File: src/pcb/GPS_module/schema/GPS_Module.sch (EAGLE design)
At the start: 8 parts, among them J1 U.FL-R-SMT-1(10), U1 SL876Q5A001T001000

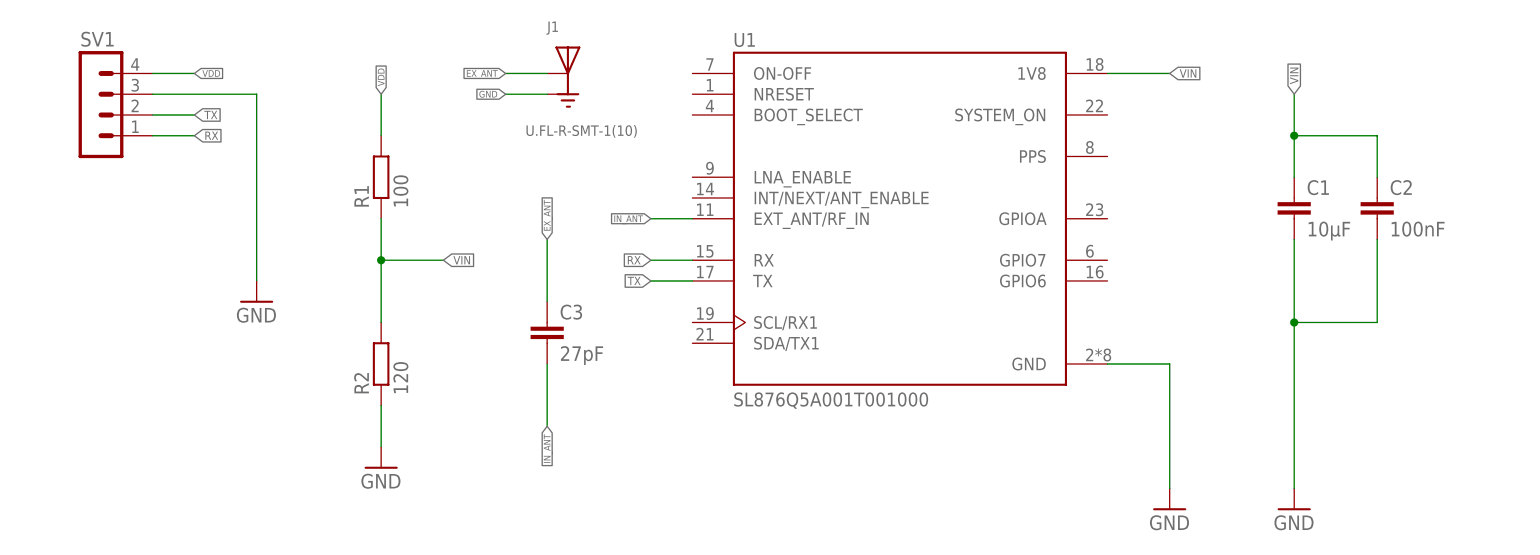
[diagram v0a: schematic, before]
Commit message: Updated GPS Module, Footprints, Automatic backups
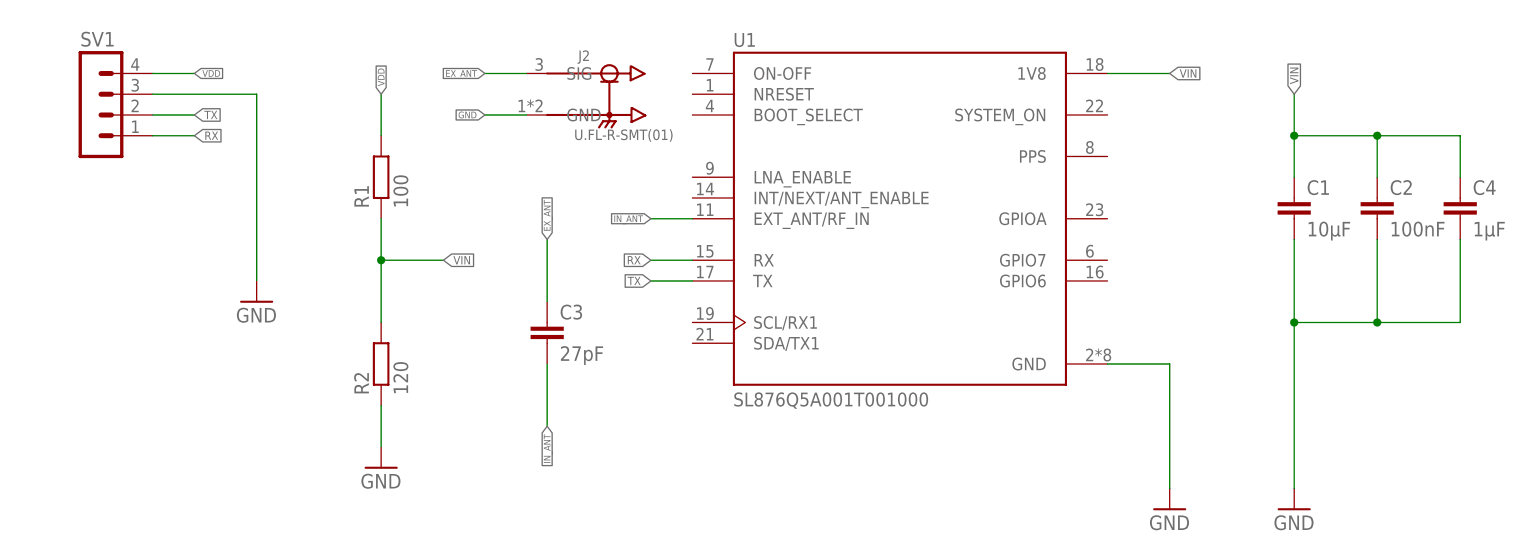
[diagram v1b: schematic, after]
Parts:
- removed J1: U.FL-R-SMT-1(10), U.FL-R-SMT-1_10_:U.FL-R-SMT-1(10)
- added C4: 1µF, rcl:C-EUC0805
- added J2: U.FL-R-SMT(01), U.FL-R-SMT_01_:U.FL-R-SMT(01)
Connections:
- net EX_ANT: now also J2.SIG; no longer J1.SIG
- net GND: now also C4.2, J2.GND; no longer J1.GND
- net VIN: now also C4.1
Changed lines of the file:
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@@
 <part name="GND4" library="supply1" library_urn="urn:adsk.eagle:library:371" deviceset="GND" device=""/>
 <part name="GND2" library="supply1" library_urn="urn:adsk.eagle:library:371" deviceset="GND" device=""/>
-<part name="J1" library="U.FL-R-SMT-1_10_" deviceset="U.FL-R-SMT-1(10)" device=""/>
 <part name="C3" library="rcl" library_urn="urn:adsk.eagle:library:334" deviceset="C-EU" device="C0805" package3d_urn="urn:adsk.eagle:package:23617/2" value="27pF"/>
+<part name="J2" library="U.FL-R-SMT_01_" deviceset="U.FL-R-SMT(01)" device=""/>
+<part name="C4" library="rcl" library_urn="urn:adsk.eagle:library:334" deviceset="C-EU" device="C0805" package3d_urn="urn:adsk.eagle:package:23617/2" value="1µF"/>
 </parts>
 <sheets>
@@
 <attribute name="VALUE" x="-119.38" y="-66.04" size="1.778" layer="96"/>
 </instance>
-<instance part="J1" gate="G$1" x="-93.98" y="-15.24" smashed="yes">
-<attribute name="NAME" x="-96.52058125" y="-10.153059375" size="1.27303125" layer="95"/>
-<attribute name="VALUE" x="-99.18773125" y="-22.87458125" size="1.27435" layer="96"/>
-</instance>
 <instance part="C3" gate="G$1" x="-96.52" y="-45.72" smashed="yes">
 <attribute name="NAME" x="-94.996" y="-45.339" size="1.778" layer="95"/>
 <attribute name="VALUE" x="-94.996" y="-50.419" size="1.778" layer="96"/>
+</instance>
+<instance part="J2" gate="G$1" x="-88.9" y="-17.78" smashed="yes">
+<attribute name="NAME" x="-92.71856875" y="-13.70686875" size="1.27285" layer="95"/>
+<attribute name="VALUE" x="-93.22781875" y="-23.3807" size="1.27288125" layer="96"/>
+</instance>
+<instance part="C4" gate="G$1" x="15.24" y="-30.48" smashed="yes">
+<attribute name="NAME" x="16.764" y="-30.099" size="1.778" layer="95"/>
+<attribute name="VALUE" x="16.764" y="-35.179" size="1.778" layer="96"/>
 </instance>
 </instances>
@@
 <pinref part="C1" gate="G$1" pin="1"/>
 <pinref part="C2" gate="G$1" pin="1"/>
+<pinref part="C4" gate="G$1" pin="1"/>
+<wire x1="15.24" y1="-27.94" x2="15.24" y2="-22.86" width="0.1524" layer="91"/>
+<wire x1="15.24" y1="-22.86" x2="5.08" y2="-22.86" width="0.1524" layer="91"/>
+<junction x="5.08" y="-22.86"/>
 </segment>
 </net>
@@
 <pinref part="C2" gate="G$1" pin="2"/>
 <pinref part="GND4" gate="1" pin="GND"/>
+<pinref part="C4" gate="G$1" pin="2"/>
+<wire x1="15.24" y1="-35.56" x2="15.24" y2="-45.72" width="0.1524" layer="91"/>
+<wire x1="15.24" y1="-45.72" x2="5.08" y2="-45.72" width="0.1524" layer="91"/>
+<junction x="5.08" y="-45.72"/>
 </segment>
 <segment>
-<pinref part="J1" gate="G$1" pin="GND"/>
-<wire x1="-96.52" y1="-17.78" x2="-101.6" y2="-17.78" width="0.1524" layer="91"/>
-<label x="-101.6" y="-17.78" size="0.8128" layer="95" rot="R180" xref="yes"/>
+<wire x1="-99.06" y1="-20.32" x2="-104.14" y2="-20.32" width="0.1524" layer="91"/>
+<label x="-104.14" y="-20.32" size="0.8128" layer="95" rot="R180" xref="yes"/>
+<pinref part="J2" gate="G$1" pin="GND"/>
 </segment>
 </net>
@@
 </segment>
 <segment>
-<pinref part="J1" gate="G$1" pin="SIG"/>
-<wire x1="-96.52" y1="-15.24" x2="-101.6" y2="-15.24" width="0.1524" layer="91"/>
-<label x="-101.6" y="-15.24" size="0.8128" layer="95" rot="R180" xref="yes"/>
+<wire x1="-99.06" y1="-15.24" x2="-104.14" y2="-15.24" width="0.1524" layer="91"/>
+<label x="-104.14" y="-15.24" size="0.8128" layer="95" rot="R180" xref="yes"/>
+<pinref part="J2" gate="G$1" pin="SIG"/>
 </segment>
 </net>

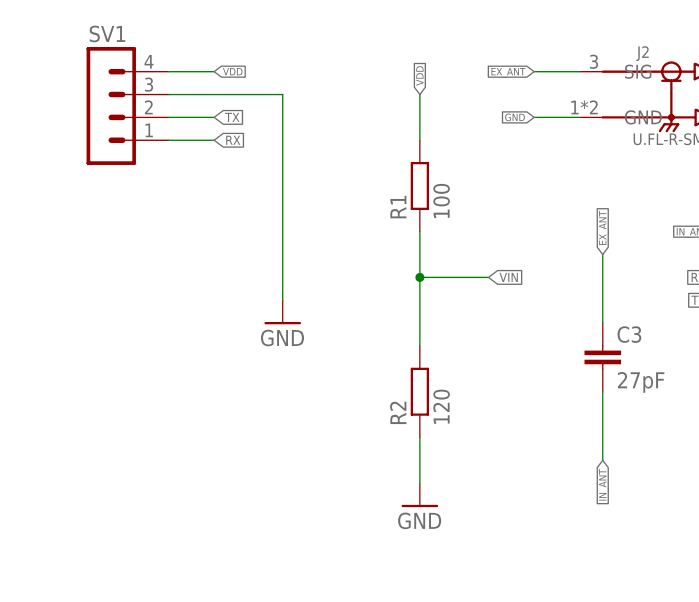
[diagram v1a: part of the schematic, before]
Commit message: updated shematic of GPS and Humidity
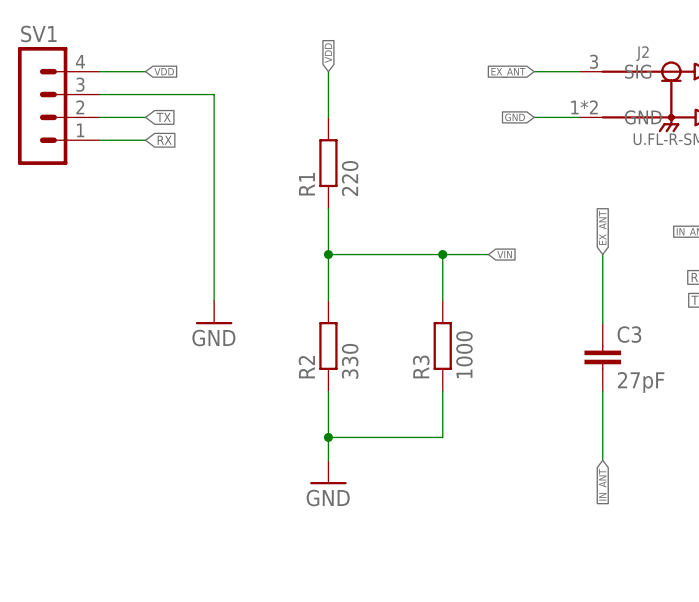
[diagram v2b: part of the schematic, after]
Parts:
- added R3: 1000, rcl:R-EU_R0402
- R1: value 100 -> 220; device rcl:R-EU_R0805 -> rcl:R-EU_R0402
- R2: value 120 -> 330; device rcl:R-EU_R0805 -> rcl:R-EU_R0402
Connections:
- net GND: now also R3.1
- net VIN: now also R3.2
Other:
- moved on the sheet: R1, R2, SV1
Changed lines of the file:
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@@
 <part name="U1" library="SL876Q5A001T001000" deviceset="SL876Q5A001T001000" device=""/>
 <part name="SV1" library="con-lstb" library_urn="urn:adsk.eagle:library:162" deviceset="MA04-1" device="" package3d_urn="urn:adsk.eagle:package:8337/1"/>
-<part name="R1" library="rcl" library_urn="urn:adsk.eagle:library:334" deviceset="R-EU_" device="R0805" package3d_urn="urn:adsk.eagle:package:23553/2" value="100"/>
-<part name="R2" library="rcl" library_urn="urn:adsk.eagle:library:334" deviceset="R-EU_" device="R0805" package3d_urn="urn:adsk.eagle:package:23553/2" value="120"/>
+<part name="R1" library="rcl" library_urn="urn:adsk.eagle:library:334" deviceset="R-EU_" device="R0402" package3d_urn="urn:adsk.eagle:package:23547/3" value="220"/>
+<part name="R2" library="rcl" library_urn="urn:adsk.eagle:library:334" deviceset="R-EU_" device="R0402" package3d_urn="urn:adsk.eagle:package:23547/3" value="330"/>
 <part name="C1" library="rcl" library_urn="urn:adsk.eagle:library:334" deviceset="C-EU" device="C0805" package3d_urn="urn:adsk.eagle:package:23617/2" value="10µF"/>
 <part name="C2" library="rcl" library_urn="urn:adsk.eagle:library:334" deviceset="C-EU" device="C0805" package3d_urn="urn:adsk.eagle:package:23617/2" value="100nF"/>
@@
 <part name="J2" library="U.FL-R-SMT_01_" deviceset="U.FL-R-SMT(01)" device=""/>
 <part name="C4" library="rcl" library_urn="urn:adsk.eagle:library:334" deviceset="C-EU" device="C0805" package3d_urn="urn:adsk.eagle:package:23617/2" value="1µF"/>
+<part name="R3" library="rcl" library_urn="urn:adsk.eagle:library:334" deviceset="R-EU_" device="R0402" package3d_urn="urn:adsk.eagle:package:23547/3" value="1000"/>
 </parts>
 <sheets>
@@
 <attribute name="VALUE" x="-73.7559" y="-55.9878" size="1.684309375" layer="96"/>
 </instance>
-<instance part="SV1" gate="1" x="-152.4" y="-17.78" smashed="yes">
-<attribute name="VALUE" x="-153.67" y="-27.94" size="1.778" layer="96"/>
-<attribute name="NAME" x="-153.67" y="-11.938" size="1.778" layer="95"/>
+<instance part="SV1" gate="1" x="-160.02" y="-17.78" smashed="yes">
+<attribute name="VALUE" x="-161.29" y="-27.94" size="1.778" layer="96"/>
+<attribute name="NAME" x="-161.29" y="-11.938" size="1.778" layer="95"/>
 </instance>
-<instance part="R1" gate="G$1" x="-116.84" y="-27.94" smashed="yes" rot="R90">
-<attribute name="NAME" x="-118.3386" y="-31.75" size="1.778" layer="95" rot="R90"/>
-<attribute name="VALUE" x="-113.538" y="-31.75" size="1.778" layer="96" rot="R90"/>
+<instance part="R1" gate="G$1" x="-127" y="-25.4" smashed="yes" rot="R90">
+<attribute name="NAME" x="-128.4986" y="-29.21" size="1.778" layer="95" rot="R90"/>
+<attribute name="VALUE" x="-123.698" y="-29.21" size="1.778" layer="96" rot="R90"/>
 </instance>
-<instance part="R2" gate="G$1" x="-116.84" y="-50.8" smashed="yes" rot="R90">
-<attribute name="NAME" x="-118.3386" y="-54.61" size="1.778" layer="95" rot="R90"/>
-<attribute name="VALUE" x="-113.538" y="-54.61" size="1.778" layer="96" rot="R90"/>
+<instance part="R2" gate="G$1" x="-127" y="-45.72" smashed="yes" rot="R90">
+<attribute name="NAME" x="-128.4986" y="-49.53" size="1.778" layer="95" rot="R90"/>
+<attribute name="VALUE" x="-123.698" y="-49.53" size="1.778" layer="96" rot="R90"/>
 </instance>
 <instance part="C1" gate="G$1" x="-5.08" y="-30.48" smashed="yes">
@@
 <attribute name="VALUE" x="6.604" y="-35.179" size="1.778" layer="96"/>
 </instance>
-<instance part="GND1" gate="1" x="-132.08" y="-43.18" smashed="yes">
-<attribute name="VALUE" x="-134.62" y="-45.72" size="1.778" layer="96"/>
+<instance part="GND1" gate="1" x="-139.7" y="-43.18" smashed="yes">
+<attribute name="VALUE" x="-142.24" y="-45.72" size="1.778" layer="96"/>
 </instance>
 <instance part="GND3" gate="1" x="-20.32" y="-68.58" smashed="yes">
@@
 <attribute name="VALUE" x="-7.62" y="-71.12" size="1.778" layer="96"/>
 </instance>
-<instance part="GND2" gate="1" x="-116.84" y="-63.5" smashed="yes">
-<attribute name="VALUE" x="-119.38" y="-66.04" size="1.778" layer="96"/>
+<instance part="GND2" gate="1" x="-127" y="-60.96" smashed="yes">
+<attribute name="VALUE" x="-129.54" y="-63.5" size="1.778" layer="96"/>
 </instance>
 <instance part="C3" gate="G$1" x="-96.52" y="-45.72" smashed="yes">
@@
 <attribute name="VALUE" x="16.764" y="-35.179" size="1.778" layer="96"/>
 </instance>
+<instance part="R3" gate="G$1" x="-114.3" y="-45.72" smashed="yes" rot="R90">
+<attribute name="NAME" x="-115.7986" y="-49.53" size="1.778" layer="95" rot="R90"/>
+<attribute name="VALUE" x="-110.998" y="-49.53" size="1.778" layer="96" rot="R90"/>
+</instance>
 </instances>
 <busses>
@@
 </segment>
 <segment>
-<wire x1="-144.78" y1="-20.32" x2="-139.7" y2="-20.32" width="0.1524" layer="91"/>
-<label x="-139.7" y="-20.32" size="1.016" layer="95" xref="yes"/>
+<wire x1="-152.4" y1="-20.32" x2="-147.32" y2="-20.32" width="0.1524" layer="91"/>
+<label x="-147.32" y="-20.32" size="1.016" layer="95" xref="yes"/>
 <pinref part="SV1" gate="1" pin="2"/>
 </segment>
@@
 <net name="VDD" class="0">
 <segment>
-<label x="-116.84" y="-17.78" size="0.8128" layer="95" rot="R90" xref="yes"/>
+<label x="-127" y="-15.24" size="0.8128" layer="95" rot="R90" xref="yes"/>
 <pinref part="R1" gate="G$1" pin="2"/>
-<wire x1="-116.84" y1="-22.86" x2="-116.84" y2="-17.78" width="0.1524" layer="91"/>
+<wire x1="-127" y1="-20.32" x2="-127" y2="-15.24" width="0.1524" layer="91"/>
 </segment>
 <segment>
-<wire x1="-144.78" y1="-15.24" x2="-139.7" y2="-15.24" width="0.1524" layer="91"/>
-<label x="-139.7" y="-15.24" size="0.8128" layer="95" xref="yes"/>
+<wire x1="-152.4" y1="-15.24" x2="-147.32" y2="-15.24" width="0.1524" layer="91"/>
+<label x="-147.32" y="-15.24" size="0.8128" layer="95" xref="yes"/>
 <pinref part="SV1" gate="1" pin="4"/>
 </segment>
@@
 </segment>
 <segment>
-<junction x="-116.84" y="-38.1"/>
-<wire x1="-116.84" y1="-33.02" x2="-116.84" y2="-38.1" width="0.1524" layer="91"/>
-<wire x1="-116.84" y1="-38.1" x2="-116.84" y2="-45.72" width="0.1524" layer="91"/>
-<wire x1="-116.84" y1="-38.1" x2="-109.22" y2="-38.1" width="0.1524" layer="91"/>
-<label x="-109.22" y="-38.1" size="1.016" layer="95" xref="yes"/>
+<wire x1="-127" y1="-30.48" x2="-127" y2="-35.56" width="0.1524" layer="91"/>
 <pinref part="R1" gate="G$1" pin="1"/>
 <pinref part="R2" gate="G$1" pin="2"/>
+<pinref part="R3" gate="G$1" pin="2"/>
+<wire x1="-127" y1="-35.56" x2="-127" y2="-40.64" width="0.1524" layer="91"/>
+<wire x1="-114.3" y1="-40.64" x2="-114.3" y2="-35.56" width="0.1524" layer="91"/>
+<wire x1="-114.3" y1="-35.56" x2="-127" y2="-35.56" width="0.1524" layer="91"/>
+<junction x="-127" y="-35.56"/>
+<junction x="-114.3" y="-35.56"/>
+<wire x1="-114.3" y1="-35.56" x2="-109.22" y2="-35.56" width="0.1524" layer="91"/>
+<label x="-109.22" y="-35.56" size="0.8128" layer="95" xref="yes"/>
 </segment>
 <segment>
@@
 <net name="RX" class="0">
 <segment>
-<wire x1="-144.78" y1="-22.86" x2="-139.7" y2="-22.86" width="0.1524" layer="91"/>
-<label x="-139.7" y="-22.86" size="1.016" layer="95" xref="yes"/>
+<wire x1="-152.4" y1="-22.86" x2="-147.32" y2="-22.86" width="0.1524" layer="91"/>
+<label x="-147.32" y="-22.86" size="1.016" layer="95" xref="yes"/>
 <pinref part="SV1" gate="1" pin="1"/>
 </segment>
@@
 <net name="GND" class="0">
 <segment>
-<wire x1="-144.78" y1="-17.78" x2="-132.08" y2="-17.78" width="0.1524" layer="91"/>
-<wire x1="-132.08" y1="-17.78" x2="-132.08" y2="-40.64" width="0.1524" layer="91"/>
+<wire x1="-152.4" y1="-17.78" x2="-139.7" y2="-17.78" width="0.1524" layer="91"/>
+<wire x1="-139.7" y1="-17.78" x2="-139.7" y2="-40.64" width="0.1524" layer="91"/>
 <pinref part="SV1" gate="1" pin="3"/>
 <pinref part="GND1" gate="1" pin="GND"/>
@@
 <segment>
 <pinref part="R2" gate="G$1" pin="1"/>
-<wire x1="-116.84" y1="-55.88" x2="-116.84" y2="-60.96" width="0.1524" layer="91"/>
+<wire x1="-127" y1="-50.8" x2="-127" y2="-55.88" width="0.1524" layer="91"/>
 <pinref part="GND2" gate="1" pin="GND"/>
+<pinref part="R3" gate="G$1" pin="1"/>
+<wire x1="-127" y1="-55.88" x2="-127" y2="-58.42" width="0.1524" layer="91"/>
+<wire x1="-114.3" y1="-50.8" x2="-114.3" y2="-55.88" width="0.1524" layer="91"/>
+<wire x1="-114.3" y1="-55.88" x2="-127" y2="-55.88" width="0.1524" layer="91"/>
+<junction x="-127" y="-55.88"/>
 </segment>
 <segment>
